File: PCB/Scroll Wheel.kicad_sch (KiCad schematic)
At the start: 37 parts, among them J1 TC2030, J2 USB_C_Receptacle_USB3.1_16P, J3 Conn_01x02_Pin, J4 Connector Encoder, J5 Connector controller, Q2 BC847, SW1 SW_Push, U1 ESP32-WROOM-E, U2 BQ25172DSGR, U6 MIC5504-3.3YM5, U7 AS5600

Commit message: Fix Git fuckup
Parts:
- added Q3: FDC6318P, Package_TO_SOT_SMD:SOT-23-6, symbol PCM_Transistor_MOSFET_AKL:FDC6318P
- added R31: 1M, Resistor_SMD:R_0402_1005Metric, symbol Device:R
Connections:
- net BATT: now also J3.2 (Pin_2), Q3.6 (D1)
- net BATT_sense_high: now also C9.2, D3.1 (K), U6.1 (VIN), U6.3 (EN), Q3.4 (D2)
- net SCL: now also J5.3 (Pin_3), R16.1
- net STATE: now also D1.1 (K), D4.1 (K)
- net at J4.2 (Pin_2), U7.8 (DIR): now also C11.1, U7.4 (GND)
- net at D5.1 (K), R26.1: now also Q3.1 (G1), Q3.3 (G2), R31.1
- net at U2.2 (ISET): now also R17.2
- net CHRG: no longer names the net of U1.9 (32K_XN/GPIO33/ADC1_CH5)
- net STDBY: no longer names the net of U1.14 (MTDI/GPIO12/ADC2_CH5)
- new net: Q3.2 (S2), Q3.5 (S1), R31.2
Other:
- moved on the sheet: D3, D5, Q2, R26, R28, SW1

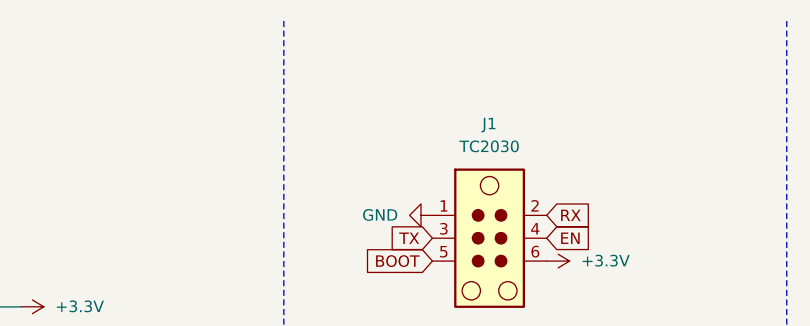
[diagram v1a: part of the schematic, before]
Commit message: add missing label
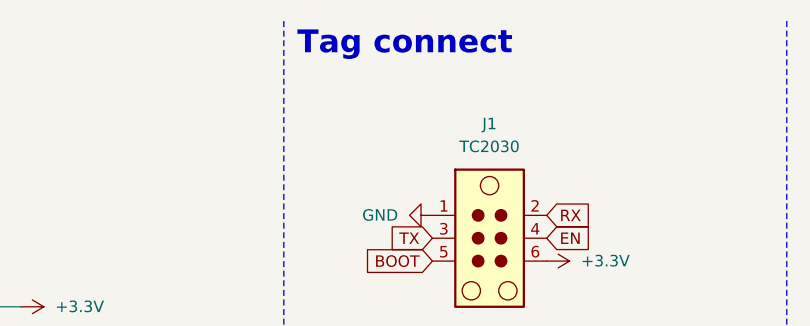
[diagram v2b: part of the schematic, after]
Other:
- note added: "Tag connect"
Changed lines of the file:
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@@
+		)
+	)
+	(text "Tag connect"
+		(exclude_from_sim no)
+		(at 252.222 15.24 0)
+		(effects
+			(font
+				(size 2.54 2.54)
+				(thickness 0.508)
+				(bold yes)
+			)
 		)
 	)

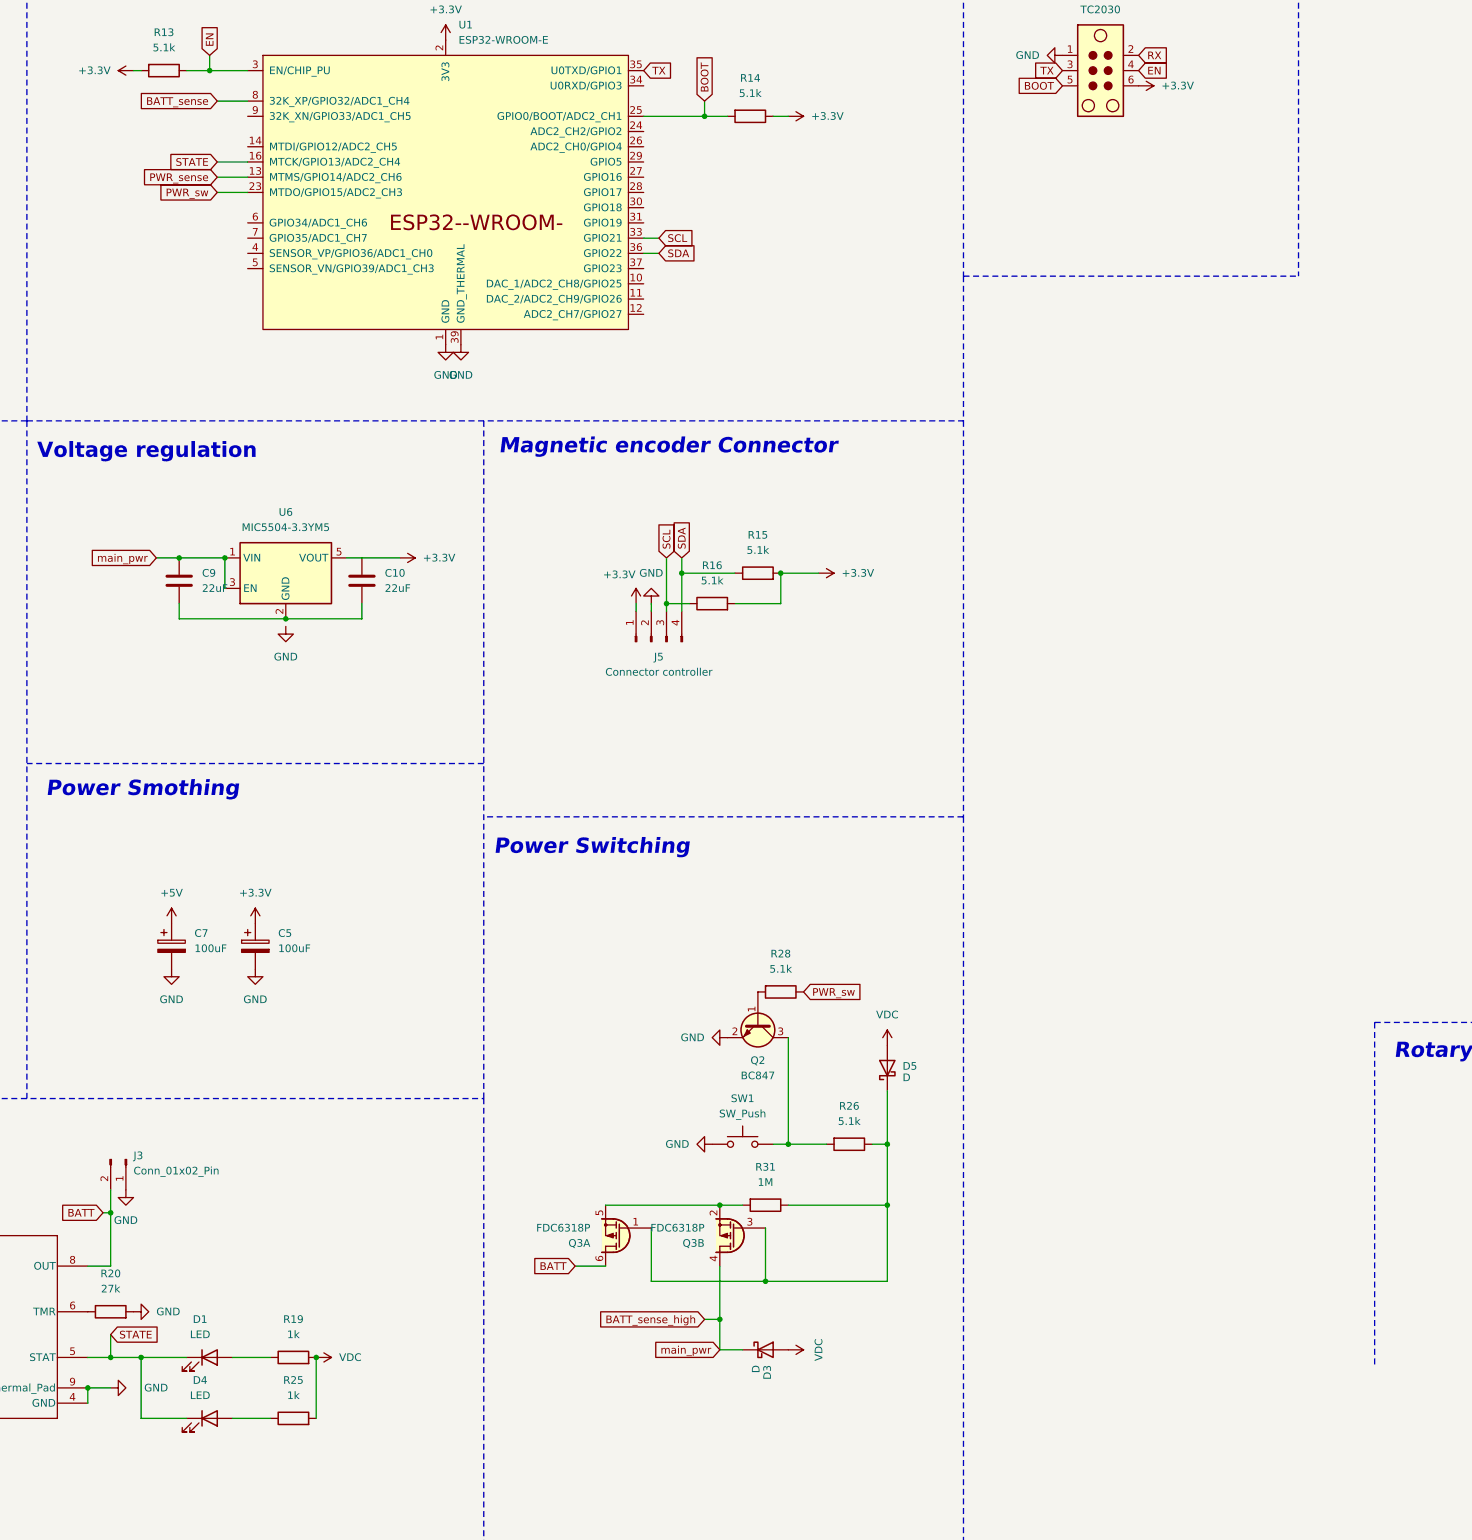
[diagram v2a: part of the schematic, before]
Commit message: replace charge state leds with power and status leds
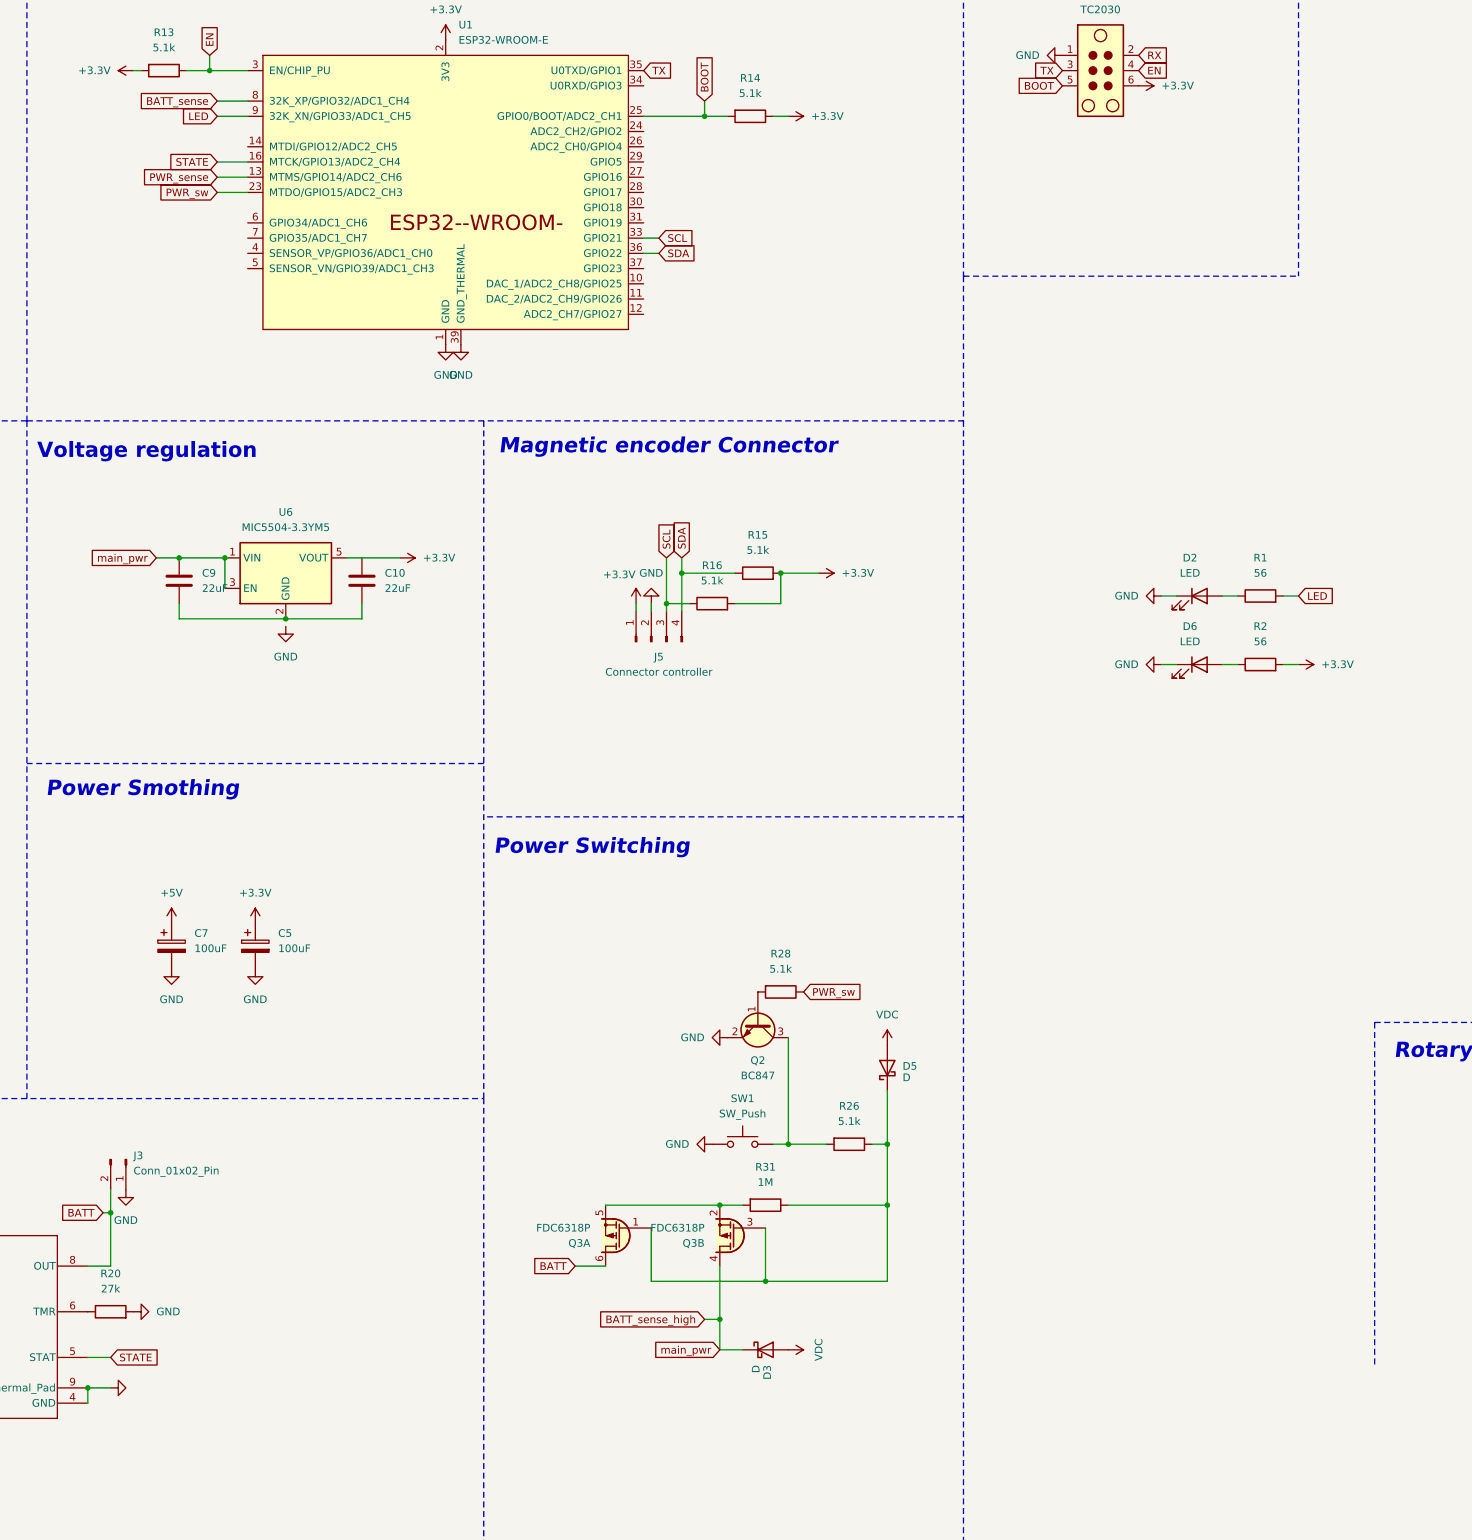
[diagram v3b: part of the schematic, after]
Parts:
- removed D1, D4: LED, PCM_Diode_SMD_AKL:D_0402_1005Metric, symbol Device:LED
- removed R19, R25: 1k, Resistor_SMD:R_0402_1005Metric, symbol Device:R
- added D2, D6: LED, PCM_Diode_SMD_AKL:D_0402_1005Metric, symbol Device:LED
- added R1, R2: 56, Resistor_SMD:R_0402_1005Metric, symbol Device:R
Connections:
- net +3.3V: now also R2.2
- net GND: now also D2.1 (K), D6.1 (K)
- net LED: now reaches U1.9 (32K_XN/GPIO33/ADC1_CH5)
- net LED: now also R1.2
- new net: D6.2 (A), R2.1
- new net: D2.2 (A), R1.1

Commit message: Fix #5
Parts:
- R17: value 330 -> 680; LCSC C105875 -> C137948
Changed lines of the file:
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@@
 		(fields_autoplaced yes)
 		(property "Reference" "R17"
-			(at 25.4 255.27 90)
+			(at 34.29 253.9999 0)
 			(effects
 				(font
 					(size 1.27 1.27)
 				)
+				(justify right)
 			)
 		)
-		(property "Value" "330"
-			(at 27.94 255.27 90)
+		(property "Value" "680"
+			(at 34.29 256.5399 0)
 			(effects
 				(font
 					(size 1.27 1.27)
 				)
+				(justify right)
 			)
 		)
@@
 			)
 		)
-		(property "LCSC" "C105875"
+		(property "LCSC" "C137948"
 			(at 31.75 255.27 0)
 			(effects

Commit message: Fix #3 and #4
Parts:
- added C1, C2: 2.2uF, Capacitor_SMD:C_0402_1005Metric, symbol Device:C
- added R3: 5.1k, Resistor_SMD:R_0402_1005Metric, symbol Device:R
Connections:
- net BATT: now also C2.1
- net GND: now also C1.1, C2.2, R3.2
- net VDC: now also C1.2
- net at U2.3 (TS): now also R3.1

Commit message: Fix #7
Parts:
- added TP1: VDC, TestPoint:TestPoint_Pad_D1.0mm, symbol Connector:TestPoint
- added TP2: GND, TestPoint:TestPoint_Pad_D1.0mm, symbol Connector:TestPoint
- added TP3: 3.3V, TestPoint:TestPoint_Pad_D1.0mm, symbol Connector:TestPoint
- added TP4: 5V, TestPoint:TestPoint_Pad_D1.0mm, symbol Connector:TestPoint
- added TP5: State, TestPoint:TestPoint_Pad_D1.0mm, symbol Connector:TestPoint
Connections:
- net +3.3V: now also TP3.1
- net +5V: now also TP4.1
- net GND: now also TP2.1
- net STATE: now also TP5.1
- net VDC: now also TP1.1
